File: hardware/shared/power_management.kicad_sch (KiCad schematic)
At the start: 28 parts, among them J3 FH12-12S-0.5SH(55), J4 1S Li-Po, U2 NPM1300-CAAA-R, U7 TPS610997

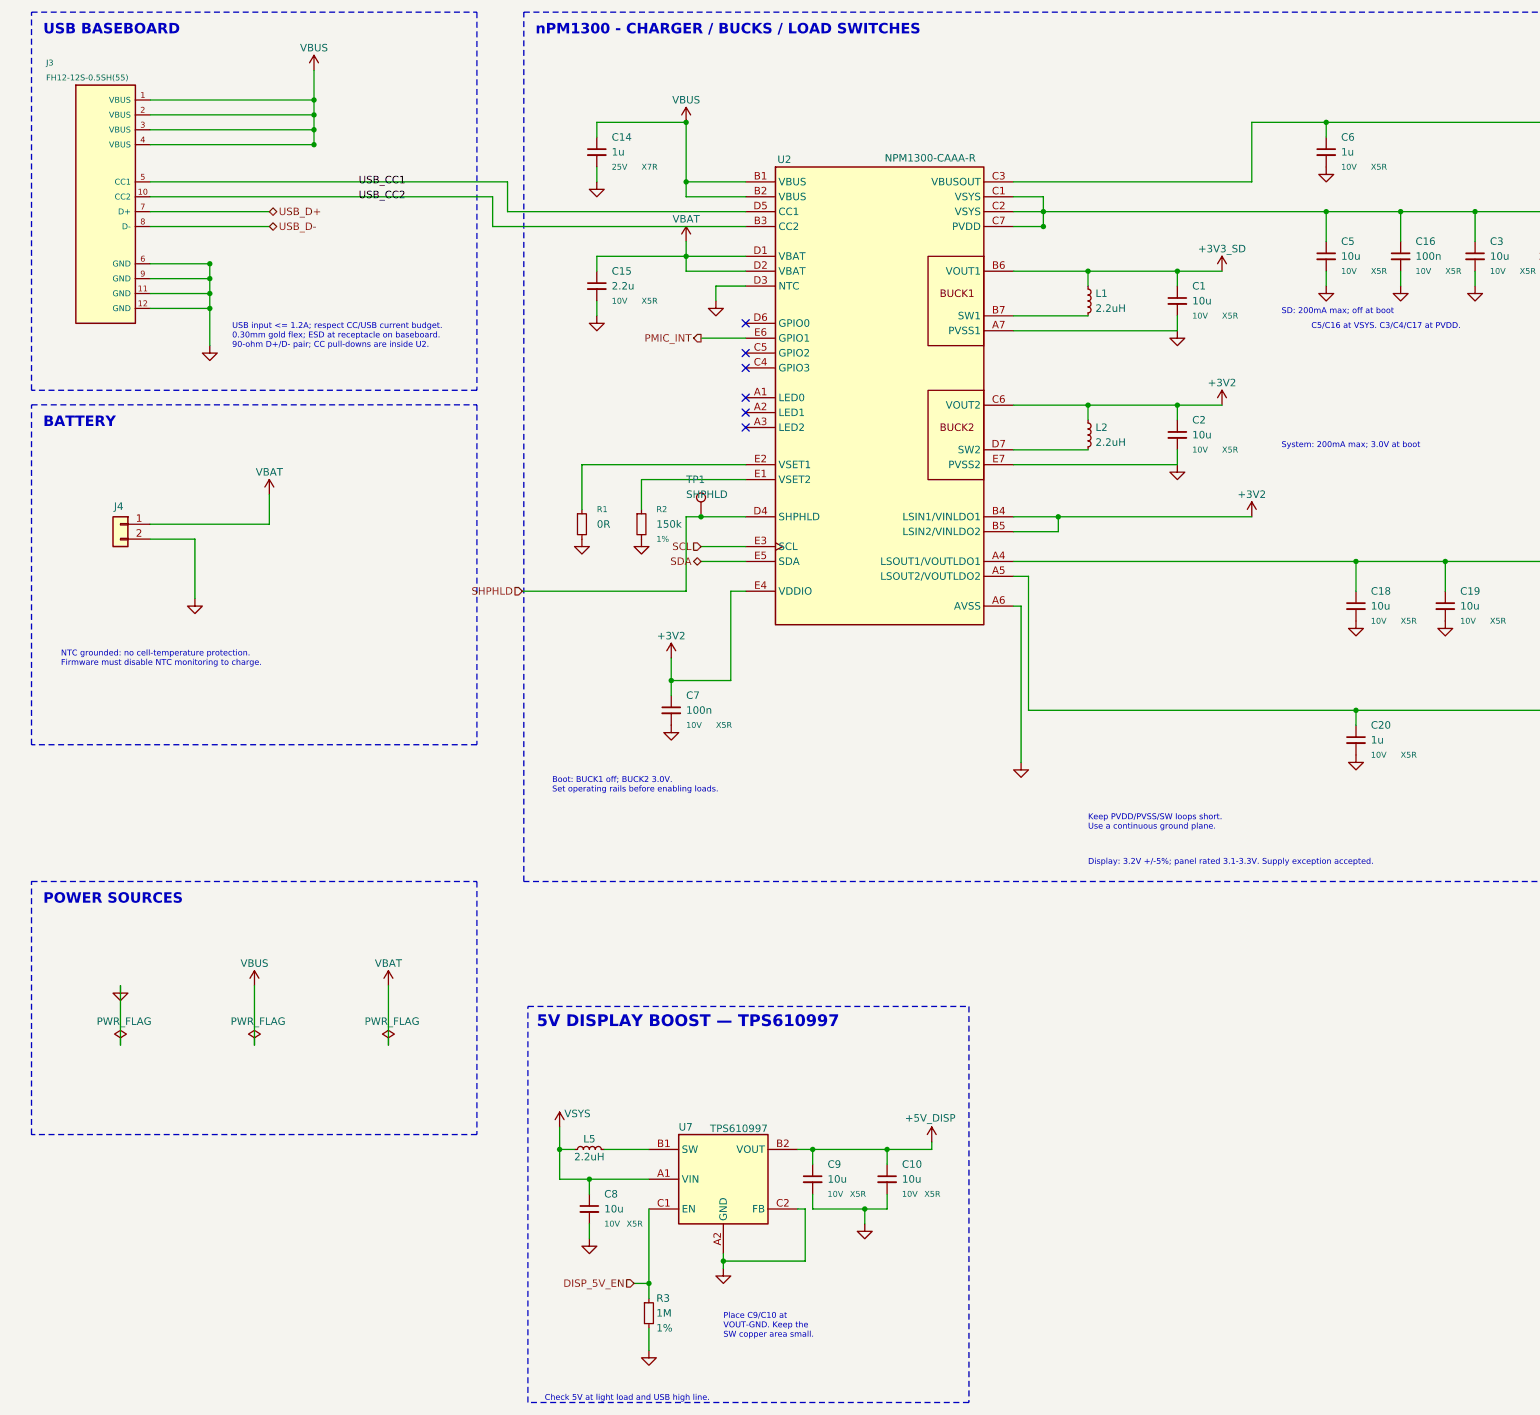
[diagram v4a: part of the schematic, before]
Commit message: fix(hardware): apply schematic review and peripheral pin mapping
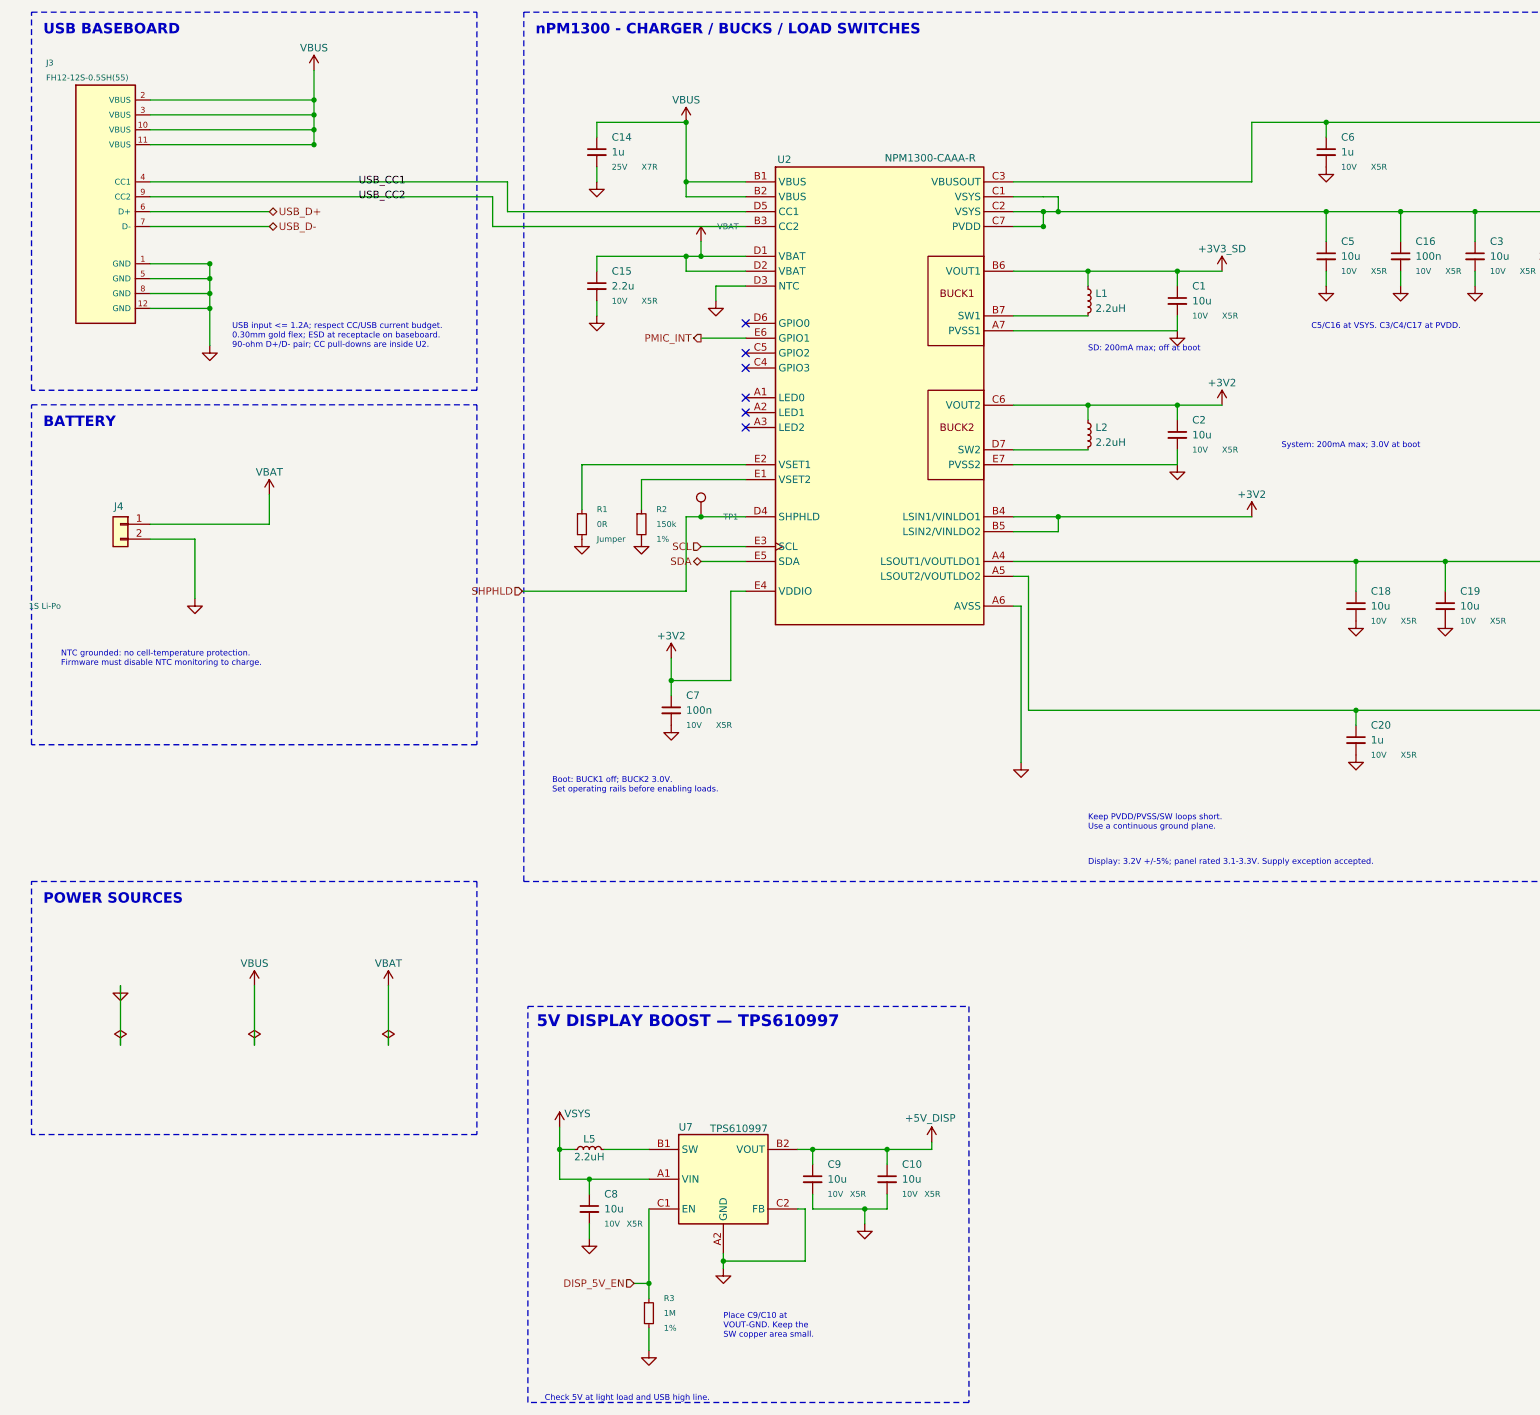
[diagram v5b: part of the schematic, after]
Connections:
- net GND: now also J3.1 (GND), J3.5 (GND), J3.8 (GND); no longer J3.11 (GND), J3.6 (GND), J3.9 (GND)
- net USB_CC1: now also J3.4 (CC1); no longer J3.5 (CC1)
- net USB_CC2: now also J3.9 (CC2); no longer J3.10 (CC2)
- net USB_D+: now also J3.6 (D+); no longer J3.7 (D+)
- net USB_D-: now also J3.7 (D-); no longer J3.8 (D-)
- net VBUS: now also J3.10 (VBUS), J3.11 (VBUS); no longer J3.1 (VBUS), J3.4 (VBUS)
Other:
- title: Power Management -> OpenBikeComputer — Power Management
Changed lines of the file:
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@@
 	(paper "A3")
 	(title_block
-		(title "Power Management")
-		(date "2026-07-18")
+		(title "OpenBikeComputer — Power Management")
 		(rev "A")
 		(company "OpenBikeComputer")
@@
 		(dnp no)
 		(property "Reference" "R3"
-			(at 134.62 251.46 0)
+			(at 135.89 251.46 0)
 			(show_name no)
 			(do_not_autoplace no)
 			(effects
 				(font
-					(size 1.27 1.27)
+					(size 1 1)
 				)
 				(justify left)
@@
 		)
 		(property "Value" "1M"
-			(at 134.62 254.0 0)
+			(at 135.89 254.0 0)
 			(show_name no)
 			(do_not_autoplace no)
 			(effects
 				(font
-					(size 1.27 1.27)
+					(size 1 1)
 				)
 				(justify left)
@@
 		)
 		(property "Tolerance" "1%"
-			(at 134.62 256.54 0)
+			(at 135.89 256.54 0)
 			(effects
 				(font
-					(size 1.27 1.27)
+					(size 1 1)
 				)
 				(justify left)
@@
 			)
 		)
-		(pin "1"
-		)
 		(pin "2"
 		)
 		(pin "3"
 		)
+		(pin "10"
+		)
+		(pin "11"
+		)
 		(pin "4"
 		)
-		(pin "5"
+		(pin "9"
 		)
-		(pin "10"
+		(pin "6"
 		)
 		(pin "7"
 		)
-		(pin "8"
-		)
-		(pin "6"
+		(pin "1"
 		)
-		(pin "9"
+		(pin "5"
 		)
-		(pin "11"
+		(pin "8"
 		)
 		(pin "12"
@@
 		)
 		(property "Value" "1S Li-Po"
-			(at 43.18 127 0)
-			(hide yes)
+			(at 33.02 133.35 0)
 			(show_name no)
 			(do_not_autoplace no)
 			(effects
 				(font
-					(size 1.27 1.27)
+					(size 1 1)
 				)
 				(justify left)
@@
 	(wire
 		(pts
-			(xy 149.86 73.66)
-			(xy 139.7 73.66)
-		)
-		(stroke
-			(width 0)
-			(type default)
-		)
-	)
-	(wire
-		(pts
 			(xy 139.7 73.66)
 			(xy 139.7 76.2)
@@
 	(symbol
 		(lib_id "obc:VBAT")
-		(at 139.7 71.12 0)
+		(at 142.24 71.12 0)
 		(unit 1)
 		(body_style 1)
@@
 		(dnp no)
 		(property "Reference" "#PWR2107"
-			(at 139.7 74.93 0)
+			(at 142.24 74.93 0)
 			(hide yes)
 			(show_name no)
@@
 		)
 		(property "Value" "VBAT"
-			(at 139.7 67.31 0)
+			(at 145.0 68.58 0)
 			(show_name no)
 			(do_not_autoplace no)
 			(effects
 				(font
-					(size 1.27 1.27)
+					(size 1 1)
 				)
+				(justify left)
 			)
 		)
 		(property "Footprint" ""
-			(at 139.7 71.12 0)
+			(at 142.24 71.12 0)
 			(hide yes)
 			(show_name no)
@@
 		)
 		(property "Datasheet" ""
-			(at 139.7 71.12 0)
+			(at 142.24 71.12 0)
 			(hide yes)
 			(show_name no)
@@
 		)
 		(property "Description" ""
-			(at 139.7 71.12 0)
+			(at 142.24 71.12 0)
 			(hide yes)
 			(show_name no)
@@
 	(wire
 		(pts
-			(xy 139.7 71.12)
-			(xy 139.7 73.66)
+			(xy 142.24 71.12)
+			(xy 142.24 73.66)
 		)
 		(stroke
@@
 	(wire
 		(pts
-			(xy 200.66 63.5)
-			(xy 200.66 66.04)
-		)
-		(stroke
-			(width 0)
-			(type default)
-		)
-	)
-	(wire
-		(pts
 			(xy 200.66 66.04)
 			(xy 195.58 66.04)
@@
 	(wire
 		(pts
-			(xy 200.66 66.04)
-			(xy 248.92 66.04)
-		)
-		(stroke
-			(width 0)
-			(type default)
-		)
-	)
-	(wire
-		(pts
 			(xy 248.92 66.04)
 			(xy 261.62 66.04)
@@
 	)
 	(text "SD: 200mA max; off at boot"
-		(at 241.3 82.55 0)
+		(at 208.28 88.9 0)
 		(effects
 			(font
@@
 		(dnp no)
 		(property "Reference" "R1"
-			(at 124.46000000000001 116.84 0)
+			(at 124.46000000000001 116.83999999999999 0)
 			(show_name no)
 			(do_not_autoplace no)
 			(effects
 				(font
-					(size 1.016 1.016)
+					(size 1 1)
 				)
 				(justify left)
@@
 			(effects
 				(font
-					(size 1.27 1.27)
+					(size 1 1)
 				)
 				(justify left)
@@
 		(property "Tolerance" "Jumper"
 			(at 124.46000000000001 121.92 0)
-			(hide yes)
 			(effects
 				(font
@@
 		(dnp no)
 		(property "Reference" "R2"
-			(at 134.62 116.84 0)
+			(at 134.62 116.83999999999999 0)
 			(show_name no)
 			(do_not_autoplace no)
 			(effects
 				(font
-					(size 1.016 1.016)
+					(size 1 1)
 				)
 				(justify left)
@@
 			(effects
 				(font
-					(size 1.27 1.27)
+					(size 1 1)
 				)
 				(justify left)
@@
 		(dnp no)
 		(property "Reference" "TP1"
-			(at 139.7 111.76 0)
+			(at 146.05 118.11 0)
 			(show_name no)
 			(do_not_autoplace no)
 			(effects
 				(font
-					(size 1.27 1.27)
+					(size 1 1)
 				)
 				(justify left)
@@
 				(justify left)
 			)
+			(hide yes)
 		)
 		(property "Footprint" "TestPoint:TestPoint_Pad_D1.0mm"
@@
 				(justify left)
 			)
+			(hide yes)
 		)
 		(property "Footprint" ""
@@
 				(justify left)
 			)
+			(hide yes)
 		)
 		(property "Footprint" ""
@@
 				(justify left)
 			)
+			(hide yes)
 		)
 		(property "Footprint" ""
@@
 		)
 	)
+	(wire
+		(pts
+			(xy 200.66 63.5)
+			(xy 203.2 63.5)
+		)
+		(stroke
+			(width 0)
+			(type default)
+		)
+	)
+	(wire
+		(pts
+			(xy 203.2 63.5)
+			(xy 203.2 66.04)
+		)
+		(stroke
+			(width 0)
+			(type default)
+		)
+	)
+	(wire
+		(pts
+			(xy 149.86 73.66)
+			(xy 142.24 73.66)
+		)
+		(stroke
+			(width 0)
+			(type default)
+		)
+	)
+	(wire
+		(pts
+			(xy 142.24 73.66)
+			(xy 139.7 73.66)
+		)
+		(stroke
+			(width 0)
+			(type default)
+		)
+	)
+	(junction
+		(at 142.24 73.66)
+		(diameter 0)
+		(color 0 0 0 0)
+	)
+	(wire
+		(pts
+			(xy 200.66 66.04)
+			(xy 203.2 66.04)
+		)
+		(stroke
+			(width 0)
+			(type default)
+		)
+	)
+	(wire
+		(pts
+			(xy 203.2 66.04)
+			(xy 248.92 66.04)
+		)
+		(stroke
+			(width 0)
+			(type default)
+		)
+	)
+	(junction
+		(at 203.2 66.04)
+		(diameter 0)
+		(color 0 0 0 0)
+	)
 )

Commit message: hardware: name critical nets and ground connector tabs
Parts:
- J4: symbol Connector_Generic:Conn_01x02 -> obc:JST_ACH_2
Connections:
- net GND: now also J3.MP (SHIELD), J4.MP (SHIELD)
- net BOOST_SW: now reaches L5.2, U7.B1 (SW)
- net PMIC_SW1: now reaches L1.2, U2.B7 (SW1)
- net PMIC_SW2: now reaches L2.2, U2.D7 (SW2)
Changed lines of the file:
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@@
 	)
 	(symbol
-		(lib_id "Connector_Generic:Conn_01x02")
+		(lib_id "obc:JST_ACH_2")
 		(at 43.18 119.38 0)
 		(mirror y)
@@
 		(dnp no)
 		(property "Reference" "J4"
-			(at 43.688 116.332 0)
+			(at 43.688 115.062 0)
 			(show_name no)
 			(do_not_autoplace no)
@@
 		)
 		(property "Value" "1S Li-Po"
-			(at 33.02 133.35 0)
+			(at 43.688 116.84 0)
 			(show_name no)
 			(do_not_autoplace no)
@@
 		)
 	)
-	(wire
-		(pts
-			(xy 55.88 121.92)
-			(xy 55.88 132.08)
-		)
-		(stroke
-			(width 0)
-			(type default)
-		)
-	)
 	(symbol
 		(lib_id "power:GND")
@@
 		(diameter 0)
 		(color 0 0 0 0)
+	)
+	(label "PMIC_SW1"
+		(at 198.12 83.82 0)
+		(effects
+			(font
+				(size 1 1)
+			)
+			(justify left bottom)
+		)
+	)
+	(label "PMIC_SW2"
+		(at 198.12 106.68 0)
+		(effects
+			(font
+				(size 1 1)
+			)
+			(justify left bottom)
+		)
+	)
+	(label "BOOST_SW"
+		(at 133.35 226.06 0)
+		(effects
+			(font
+				(size 1 1)
+			)
+			(justify right bottom)
+		)
+	)
+	(wire
+		(pts
+			(xy 40.64 88.9)
+			(xy 58.42 88.9)
+		)
+		(stroke
+			(width 0)
+			(type default)
+		)
+	)
+	(junction
+		(at 58.42 88.9)
+		(diameter 0)
+		(color 0 0 0 0)
+	)
+	(wire
+		(pts
+			(xy 43.18 125.73)
+			(xy 55.88 125.73)
+		)
+		(stroke
+			(width 0)
+			(type default)
+		)
+	)
+	(wire
+		(pts
+			(xy 55.88 121.92)
+			(xy 55.88 125.73)
+		)
+		(stroke
+			(width 0)
+			(type default)
+		)
+	)
+	(wire
+		(pts
+			(xy 55.88 125.73)
+			(xy 55.88 132.08)
+		)
+		(stroke
+			(width 0)
+			(type default)
+		)
+	)
+	(junction
+		(at 55.88 125.73)
+		(diameter 0)
+		(color 0 0 0 0)

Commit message: hardware: prepare QFN schematic for non-HDI boards
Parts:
- removed C18, C19: 10u, Capacitor_SMD:C_0805_2012Metric, symbol Device:C_Small
- added Q1: AO3400A, Package_TO_SOT_SMD:SOT-23, symbol Transistor_FET:AO3400A
- added R63, R65: 36.5k, Resistor_SMD:R_0402_1005Metric, symbol Device:R_Small
- added R64: 10.5k, Resistor_SMD:R_0402_1005Metric, symbol Device:R_Small
- added R66: 1k, Resistor_SMD:R_0402_1005Metric, symbol Device:R_Small
- added R67: 100k, Resistor_SMD:R_0402_1005Metric, symbol Device:R_Small
- C1, C2: Capacitance budget (none) -> PROVISIONAL: 4-20uF effective total per buck rail, includin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; Selection reference (none) -> https://docs.nordicsemi.com/r/bundle/nwp_050/page/wp/nwp_05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
- C10, C9: value 10u -> 22u; Capacitance at bias Minimum 5uF at 5.2V over tolerance and temperature -> >=5uF effective at 5.15V over tolerance and temperature
- C8: Capacitance at bias Minimum 1uF at 5.5V over tolerance and temperature -> >=5uF effective at 5.5V over tolerance and temperature
- R1: Tolerance Jumper -> 1%
- R3: MPN RC0402FR-071ML -> (none); Manufacturer Yageo -> (none)
- U2: value NPM1300-CAAA-R -> nPM1300-QEAA; footprint obc:BGA35N44X41P5X7_237X307X51 -> Package_DFN_QFN:QFN-32-1EP_5x5mm_P0.5mm_EP3.6x3.6mm; symbol obc:NPM1300-CAAA-R -> obc:nPM1300-QEAA; License (none) -> CERN-OHL-P-2.0; hardware/libraries/LICENSE.nordic-lib-kicad; MAXIMUM_PACKAGE_HEIGHT 0.512mm -> (none); MPN NPM1300-CAAA-R -> NPM1300-QEAA-R; PARTREV v1.1 -> (none); STANDARD IPC-7.51B -> (none); Source (none) -> https://github.com/hlord2000/nordic-lib-kicad/tree/05a4dae2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
- U7: value TPS610997 -> TPS63900DSKR; footprint obc:TI_YFF0006_0.884x1.226mm_P0.4mm -> Package_SON:WSON-10-1EP_2.5x2.5mm_P0.5mm_EP1.2x2mm; symbol obc:TPS610997 -> obc:TPS63900DSKR; MPN TPS610997YFFR -> TPS63900DSKR
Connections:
- net +3V2: now also U2.12 (VDDIO), U2.30 (LSIN2/VINLDO2), U2.32 (VOUT2); no longer U2.B4 (LSIN1/VINLDO1), U2.B5 (LSIN2/VINLDO2), U2.C6 (VOUT2), U2.E4 (VDDIO)
- net +3V2_GPS: now also U2.31 (LSOUT2/VOUTLDO2); no longer U2.A5 (LSOUT2/VOUTLDO2)
- net +3V3_SD: now also U2.1 (VOUT1); no longer U2.B6 (VOUT1)
- net +5V_DISP: now also U7.6 (VOUT), R66.1; no longer U7.B2 (VOUT)
- net DISP_5V_EN: now also U2.7 (GPIO0), U7.1 (EN); no longer U7.C1 (EN)
- net GND: now also U2.18 (NTC), U2.2 (PVSS1), U2.28 (LSIN1/VINLDO1), U2.29 (LSOUT1/VOUTLDO1), U2.33 (AVSS), U2.6 (PVSS2), U7.11 (GND), U7.2 (SEL), U7.8 (GND), Q1.2 (S), R63.2, R64.2, R65.2, R67.2; no longer U2.A6 (AVSS), U2.A7 (PVSS1), U2.D3 (NTC), U2.E7 (PVSS2), U7.A2 (GND), U7.C2 (FB)
- net PMIC_INT: now also U2.8 (GPIO1); no longer U2.E6 (GPIO1)
- net SCL: now also U2.14 (SCL); no longer U2.E3 (SCL)
- net SDA: now also U2.13 (SDA); no longer U2.E5 (SDA)
- net SHPHLD: now also U2.15 (SHPHLD); no longer U2.D4 (SHPHLD)
- net USB_VBUS: now also U2.22 (VBUSOUT); no longer U2.C3 (VBUSOUT)
- net VBAT: now also U2.19 (VBAT); no longer U2.D1 (VBAT), U2.D2 (VBAT)
- net VBUS: now also U2.21 (VBUS); no longer U2.B1 (VBUS), U2.B2 (VBUS)
- net VSYS: now also U2.20 (VSYS), U2.4 (PVDD), U7.10 (VIN); no longer L5.1, U2.C1 (VSYS), U2.C2 (VSYS), U2.C7 (PVDD), U7.A1 (VIN)
- net at R2.1: now also U2.16 (VSET2); no longer U2.E1 (VSET2)
- net at R1.1: now also U2.17 (VSET1); no longer U2.E2 (VSET1)
- removed net +1V8_MAG: U2.A4 (LSOUT1/VOUTLDO1)
- net BOOST_SW: no longer names the net of L5.2
- net BOOST_SW: now also U7.7 (LX2); no longer U7.B1 (SW)
- net PMIC_SW1: no longer names the net of L1.2
- net PMIC_SW1: now also U2.3 (SW1); no longer U2.B7 (SW1)
- net PMIC_SW2: no longer names the net of L2.2
- net PMIC_SW2: now also U2.5 (SW2); no longer U2.D7 (SW2)
- net USB_CC1: no longer names the net of J3.4 (CC1)
- net USB_CC1: now also U2.23 (CC1); no longer U2.D5 (CC1)
- net USB_CC2: no longer names the net of J3.9 (CC2)
- net USB_CC2: now also U2.24 (CC2); no longer U2.B3 (CC2)
- new net: R63.1, U7.3 (CFG1)
- new net: R64.1, U7.4 (CFG2)
- new net: R65.1, U7.5 (CFG3)
- new net: L5.1, U7.9 (LX1)
- new net: Q1.3 (D), R66.2
- new net COM_EN: U2.9 (GPIO2)
- new net DISP_DISCHARGE: Q1.1 (G), R67.1, U2.11 (GPIO4)
- new net LOUD: U2.10 (GPIO3)
- no-connect marks 6 -> 3
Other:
- note added: "5V DISPLAY / BUCK-BOOST"
- note added: "BUCK1: off at boot; set 3.3V for SD. BUCK2: 3.0V at boot; set 3.2V before LCD enable. LS1 unused: both pins grounded, keep disabled. LS2: +3V2_GPS; 50mA soft-start target."
- note added: "Buck capacitor population is provisional: target 4-20uF effective per whole rail. Select actual MLCCs, include LS2 off/on, and verify start-up and rail droop."
- note added: "C5/C16 at VSYS; C3/C4/C17 at PVDD. C7 at VDDIO (12). PVSS1/2 need separate vias. Solder AVSS pad 33. LS1 must remain disabled. LED0: fault; LED1: charge; LED2: host (unfitted)."
- note added: "CFG1/3 = 36.5k; CFG2 = 10.5k: both presets 5.0V, 100mA input limit. C8 >=5uF effective; C9+C10 >=10uF effective. Keep L5 at 2.2uH. Recheck input limit when the backlight is selected."
- note added: "CHARGER / BUCKS / SWITCHED GNSS"
- note added: "COMMANDED VDD2 DISCHARGE"
- note added: "Display rail qualification: BUCK2 3.2V +/-5% exceeds the panel 3.1-3.3V window. Check both rails across supply, load and temperature. Wait for 5V to settle before the Sharp start sequence; TPS63900 start-up is about 6ms typical, not a bound."
- note added: "GPIO4 high discharges VDD2 after U7 is disabled. Verify VDD2 fall before removing VDD1. An abrupt PMIC reset or power loss bypasses this software sequence and needs bench qualification."
- note added: "USB / BATTERY"
- note added: "USB input <=1.2A; obey CC / USB current budget. ESD is on the USB baseboard. CC pulls are in U2. Battery polarity and charge current need pack approval. NTC grounded: no pack-temperature protection."
- note removed: "5V DISPLAY BOOST — TPS610997"
- note removed: "BATTERY"
- note removed: "Boot: BUCK1 off; BUCK2 3.0V. Set operating rails before enabling loads."
- note removed: "C5/C16 at VSYS. C3/C4/C17 at PVDD."
- note removed: "Check 5V at light load and USB high line."
- note removed: "Display: 3.2V +/-5%; panel rated 3.1-3.3V. Supply exception accepted."
- note removed: "GPS switch: 100mA max; off at boot"
- note removed: "Keep PVDD/PVSS/SW loops short. Use a continuous ground plane."
- note removed: "LDO1: 1.8V, 50mA max; off at boot"
- note removed: "NTC grounded: no cell-temperature protection. Firmware must disable NTC monitoring to charge."
- note removed: "POWER SOURCES"
- note removed: "Place C9/C10 at VOUT-GND. Keep the SW copper area small."
- note removed: "SD: 200mA max; off at boot"
- note removed: "System: 200mA max; 3.0V at boot"
- note removed: "USB BASEBOARD"
- note removed: "USB input <= 1.2A; respect CC/USB current budget. 0.30mm gold flex; ESD at receptacle on baseboard. 90-ohm D+/D- pair; CC pull-downs are inside U2."
- note removed: "nPM1300 - CHARGER / BUCKS / LOAD SWITCHES"
- title: OpenBikeComputer — Power Management -> OpenBikeComputer - QFN power management
- moved on the sheet: C1, C10, C14, C15, C16, C17, C2, C20, C3, C4, C5, C6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
